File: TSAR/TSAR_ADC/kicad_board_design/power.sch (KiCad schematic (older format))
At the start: 16 parts, among them U1 LTC3260, U2 LM78L05ACZ_NOPB

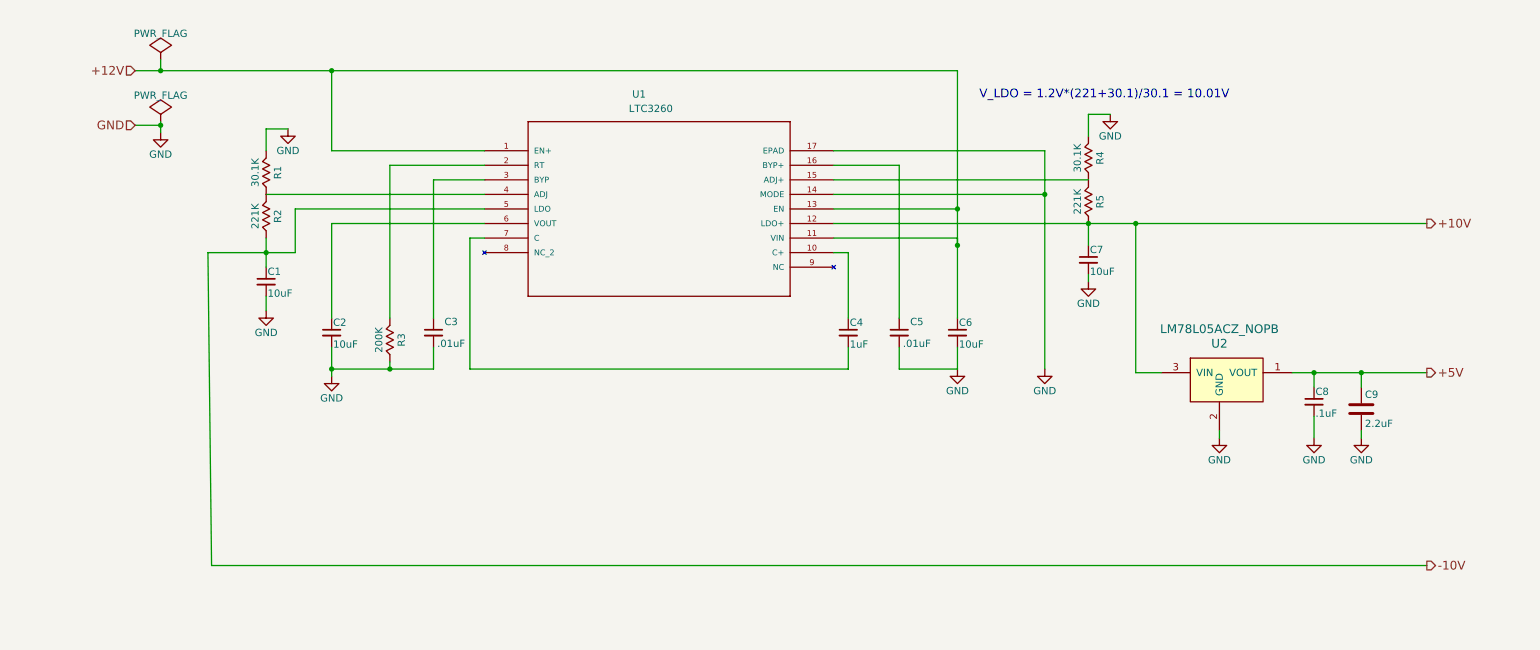
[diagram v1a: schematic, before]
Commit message: Simplify thermocouple signal chain for better worst case.
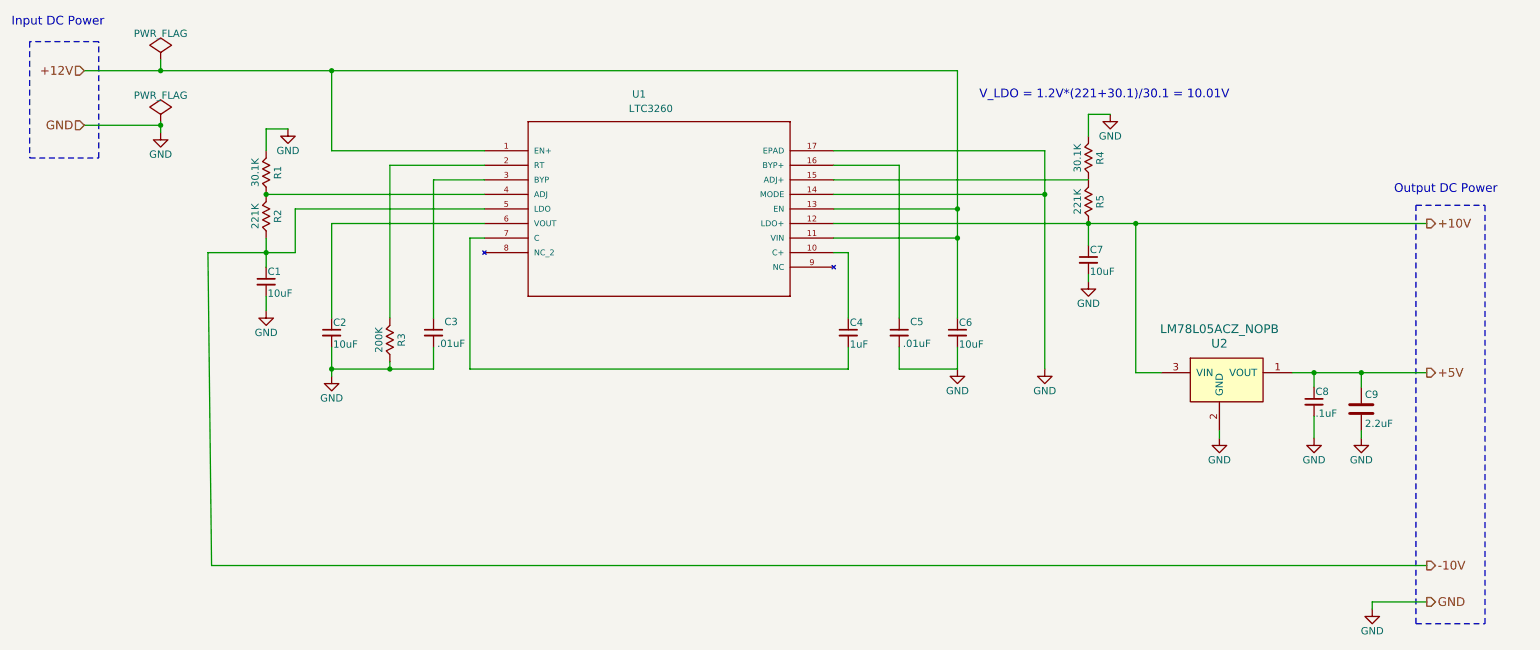
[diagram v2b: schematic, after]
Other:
- note added: "Input DC Power"
- note added: "Output DC Power"
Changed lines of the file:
@@
 Text Notes 7275 2350 0    60   ~ 0
 V_LDO = 1.2V*(221+30.1)/30.1 = 10.01V
-Text HLabel 1475 2150 0    60   Input ~ 0
+Text HLabel 1125 2150 0    60   Input ~ 0
 +12V
 Text HLabel 10350 3200 2    60   Output ~ 0
@@
 Text HLabel 10350 4225 2    60   Output ~ 0
 +5V
-Text HLabel 1475 2525 0    60   Input ~ 0
+Text HLabel 1125 2525 0    60   Input ~ 0
 GND
 Wire Wire Line
 	2825 2700 3875 2700
 Wire Wire Line
-	1475 2150 7125 2150
+	1125 2150 7125 2150
 Wire Wire Line
 	7125 3100 6275 3100
@@
 	6275 3300 7125 3300
 Wire Wire Line
-	7125 3300 7125 3350
-Wire Wire Line
 	7125 4050 7125 4200
 Wire Wire Line
@@
 	9900 4325 9900 4225
 Wire Wire Line
-	1475 2525 1650 2525
+	1125 2525 1650 2525
 Wire Wire Line
 	1650 2500 1650 2575
 Connection ~ 2825 2150
 Connection ~ 7125 3100
-Connection ~ 7125 3350
+Connection ~ 7125 3300
 Connection ~ 7725 3000
 Connection ~ 2375 3400
@@
 	1650 2075 1650 2150
 Connection ~ 1650 2150
+Connection ~ 2375 3000
+Text Notes 625  1850 0    60   ~ 0
+Input DC Power
+Text Notes 10125 3000 0    60   ~ 0
+Output DC Power
+Wire Notes Line
+	750  1950 750  2750
+Wire Notes Line
+	750  2750 1225 2750
+Wire Notes Line
+	1225 2750 1225 1950
+Wire Notes Line
+	1225 1950 750  1950
+$Comp
+L GND #PWR?
+U 1 1 5BDF5727
+P 9975 5850
+F 0 "#PWR?" H 9975 5600 50  0001 C CNN
+F 1 "GND" H 9975 5700 50  0000 C CNN
+F 2 "" H 9975 5850 50  0000 C CNN
+F 3 "" H 9975 5850 50  0000 C CNN
+	1    9975 5850
+	1    0    0    -1
+$EndComp
+Text HLabel 10350 5800 2    60   Output ~ 0
+GND
+Wire Wire Line
+	9975 5850 9975 5800
+Wire Wire Line
+	9975 5800 10350 5800
+Wire Notes Line
+	10275 5950 10750 5950
+Wire Notes Line
+	10275 5950 10275 3075
+Wire Notes Line
+	10275 3075 10750 3075
+Wire Notes Line
+	10750 3075 10750 5950
 $EndSCHEMATC
